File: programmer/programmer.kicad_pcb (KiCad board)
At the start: 2 copper layers, 62.2 x 54 mm, 5 parts, among them J1 v1 programmer, J2 v2 programmer

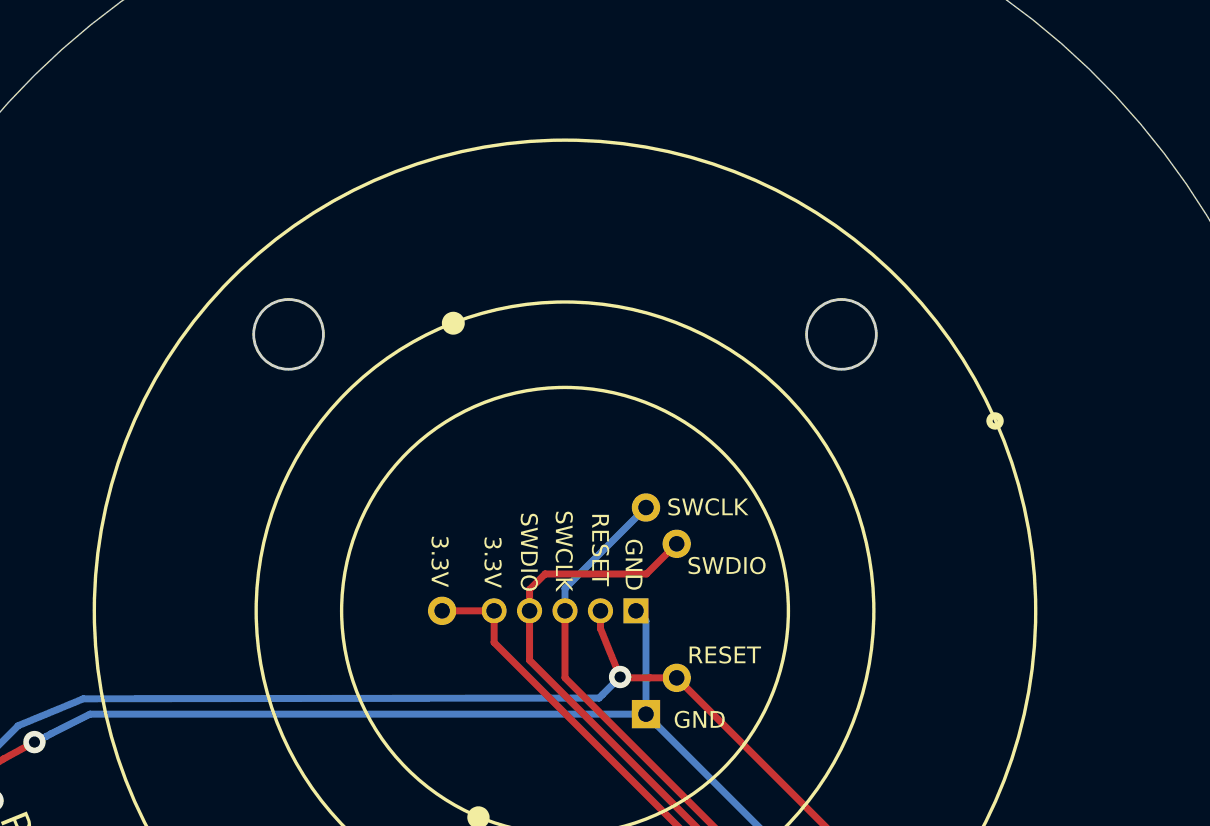
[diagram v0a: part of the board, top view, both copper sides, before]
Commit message: update programmer rig to have space for a the bar pin attachments I've been using, otherwise once a bar pin is attached the programmer rig can no longer be used
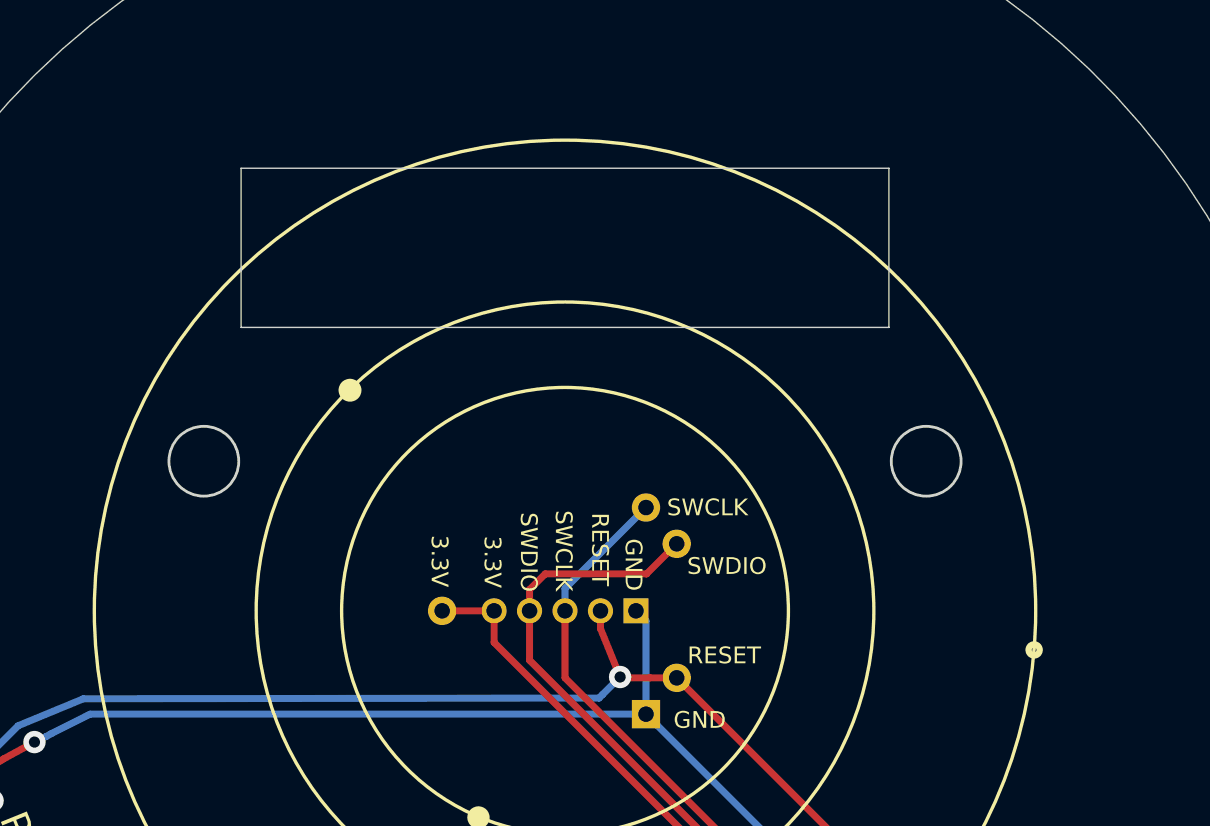
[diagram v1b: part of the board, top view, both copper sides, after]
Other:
- outline, holes or cut-outs redrawn
